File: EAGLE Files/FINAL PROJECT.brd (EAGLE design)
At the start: 96.5 x 48.3 mm, 11 parts, among them J1 BATTERY, U1 9_to_3.3_VREG

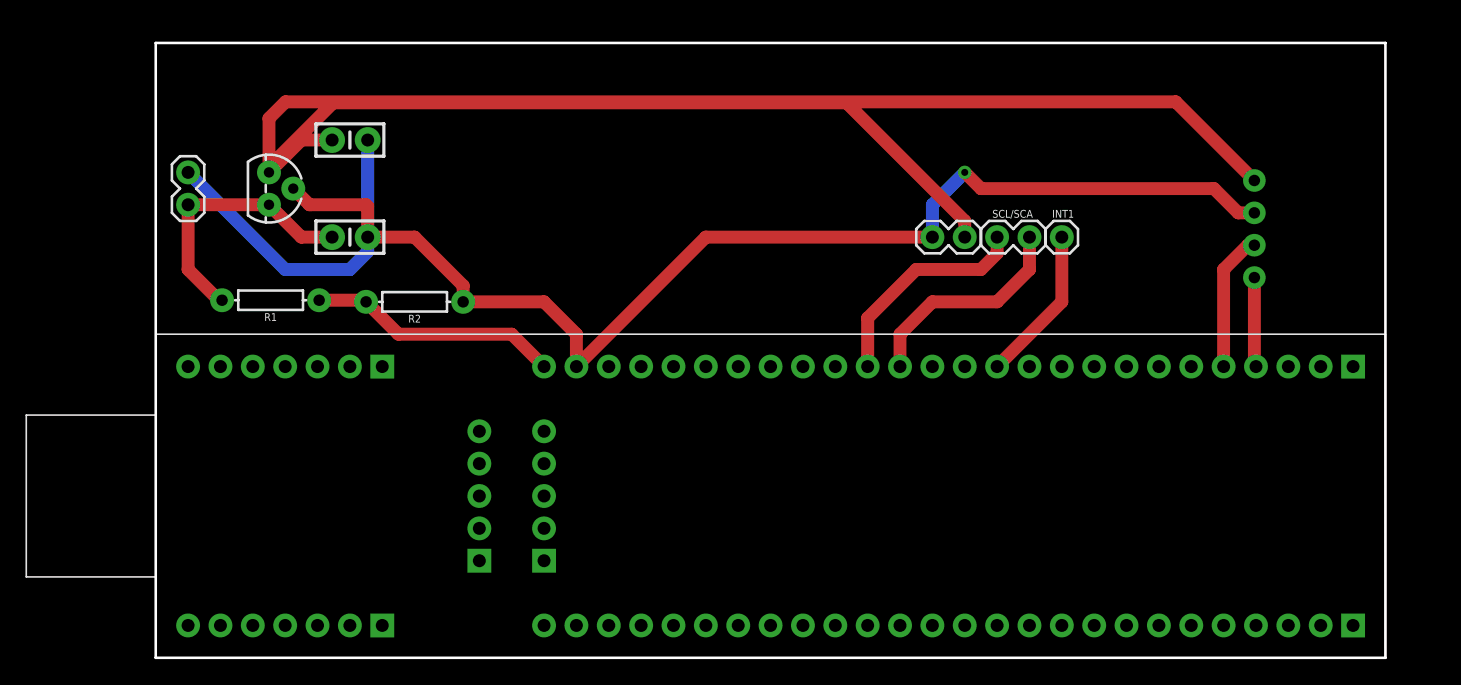
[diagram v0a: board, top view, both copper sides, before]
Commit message: EAGLE-Files-added LED
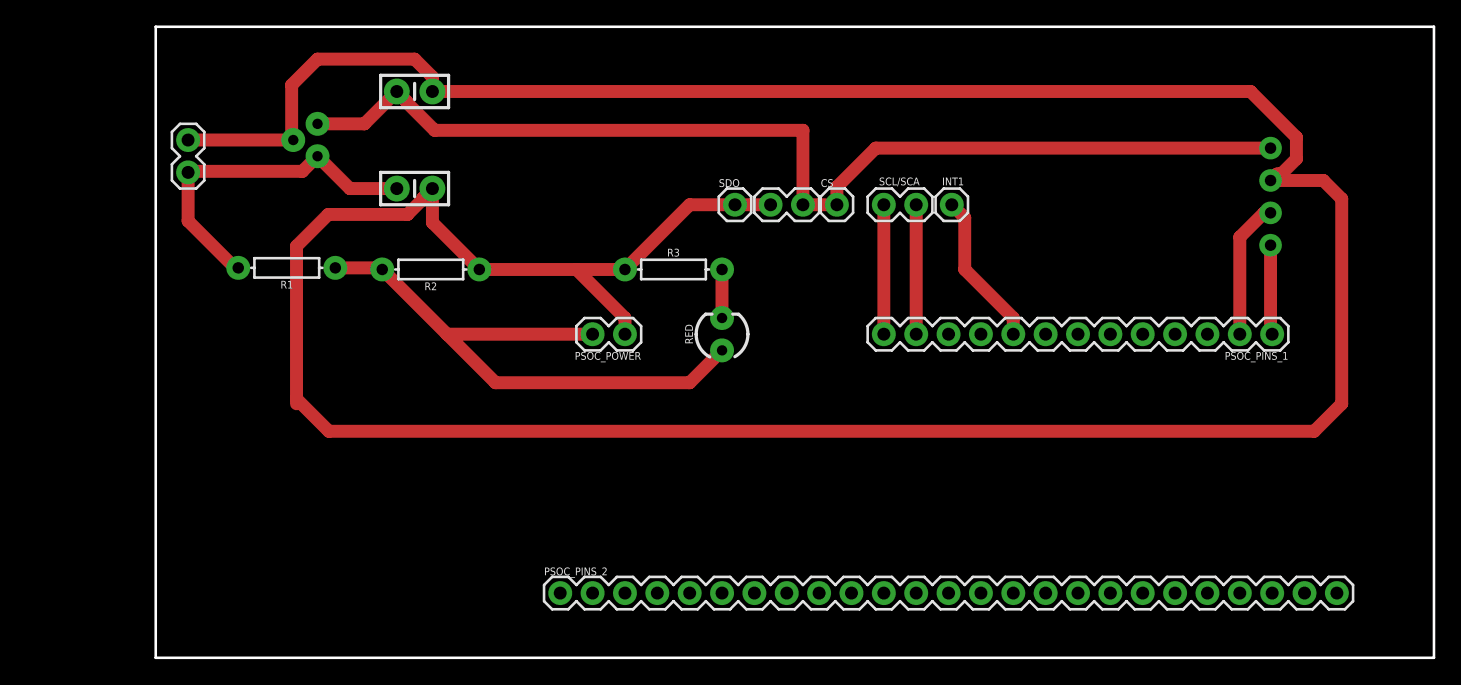
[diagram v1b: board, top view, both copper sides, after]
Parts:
- removed U$1: CY8CKIT-059, CYKIT:CY8CKIT-059
- added CS, SDO: (no value), SparkFun-Connectors:1X01
- added PSOC_PINS_1: (no value), SparkFun-Connectors:1X13
- added PSOC_PINS_2: (no value), SparkFun-Connectors:1X25
- added PSOC_POWER: (no value), SparkFun-Connectors:1X02
- added R3: 330, SparkFun-Resistors:AXIAL-0.3
- added RED: (no value), SparkFun-LED:LED_3MM
- moved GND/VDD 13.0 mm to (48.3, 35.6)
- moved SCL/SCA 9.25 mm to (57.1, 35.6)
- moved INT1 9.00 mm to (62.5, 35.6)
- moved C3 6.35 mm to (20.3, 44.5)
- moved C4 6.35 mm to (20.3, 36.8)
- moved U1 5.39 mm to (12.7, 40.6), flipped to the bottom
- moved HC-05 2.84 mm to (104.0, 36.2)
- moved R1 2.84 mm to (10.3, 30.6)
- moved R2 2.84 mm to (21.6, 30.5)
- moved J1 2.54 mm to (2.54, 40.6)
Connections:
- new net N$1: R3.P$2, RED.K
- net 5V: now also PSOC_POWER.2, RED.A; no longer U$1.26
- net GND: now also PSOC_POWER.1, R3.P$1, SDO.1; no longer U$1.25
- net INT1: now also PSOC_PINS_1.9; no longer U$1.12
- net RX: now also PSOC_PINS_1.1; no longer U$1.4
- net SCA: now also PSOC_PINS_1.12; no longer U$1.15
- net SCL: now also PSOC_PINS_1.13; no longer U$1.16
- net TX: now also PSOC_PINS_1.2; no longer U$1.5
- net VDD: now also CS.1
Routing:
- net GND: track 120.6 -> 271.0 mm, vias 1 -> 0
- net VDD: track 152.9 -> 85.7 mm
- net 5V: track 19.8 -> 46.6 mm
- net SCL: track 17.3 -> 10.2 mm
- net SCA: track 17.3 -> 10.2 mm
- net VDD1: track 21.1 -> 27.2 mm
- net N$1: track 0.00 -> 3.81 mm
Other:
- board size 96.5 x 48.3 mm -> 100.3 x 49.5 mm
